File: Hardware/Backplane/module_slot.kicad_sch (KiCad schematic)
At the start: 29 parts, among them J402 10018784-10201TLF, Q401 S3134K, Q402 GSF3407, Q403 GSF3407, Q404 GSF3407, U401 NL17SZS11DFT2G-Q

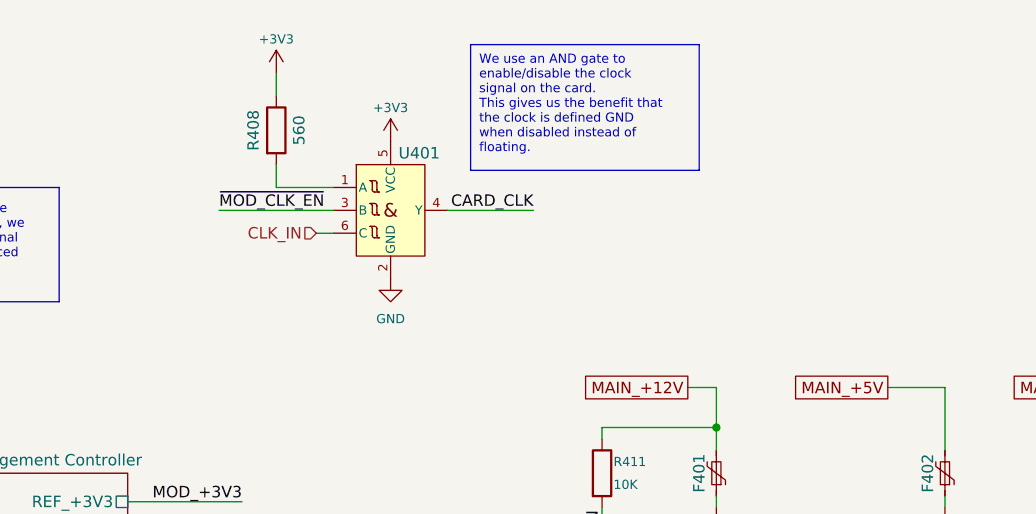
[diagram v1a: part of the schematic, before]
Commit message: Fixes several issues with the backplane schematic.
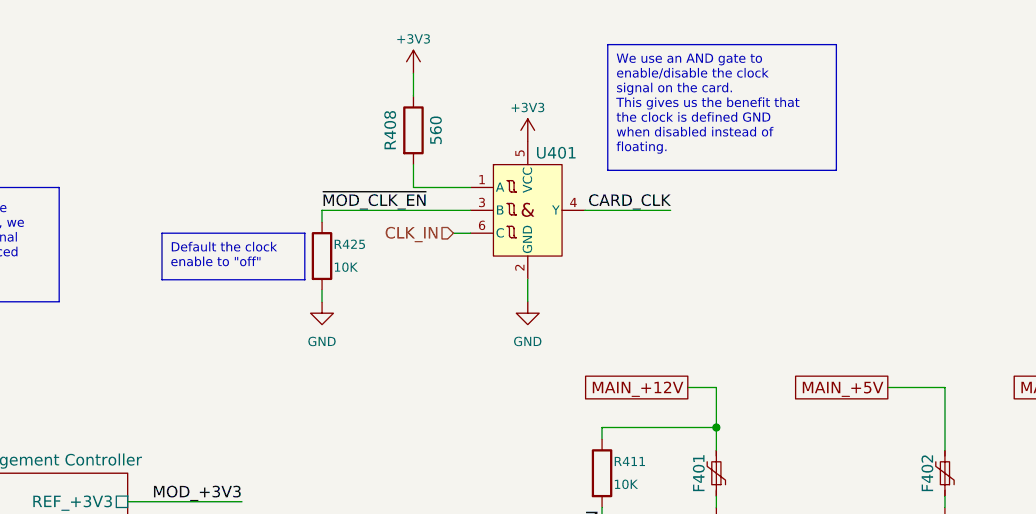
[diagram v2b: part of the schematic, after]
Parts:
- added R425: 10K, Resistor_SMD:R_0603_1608Metric, symbol Device:R
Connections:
- net GND: now also R425.2
- net ~{MOD_CLK_EN}: now also R425.1
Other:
- moved on the sheet: R408, U401

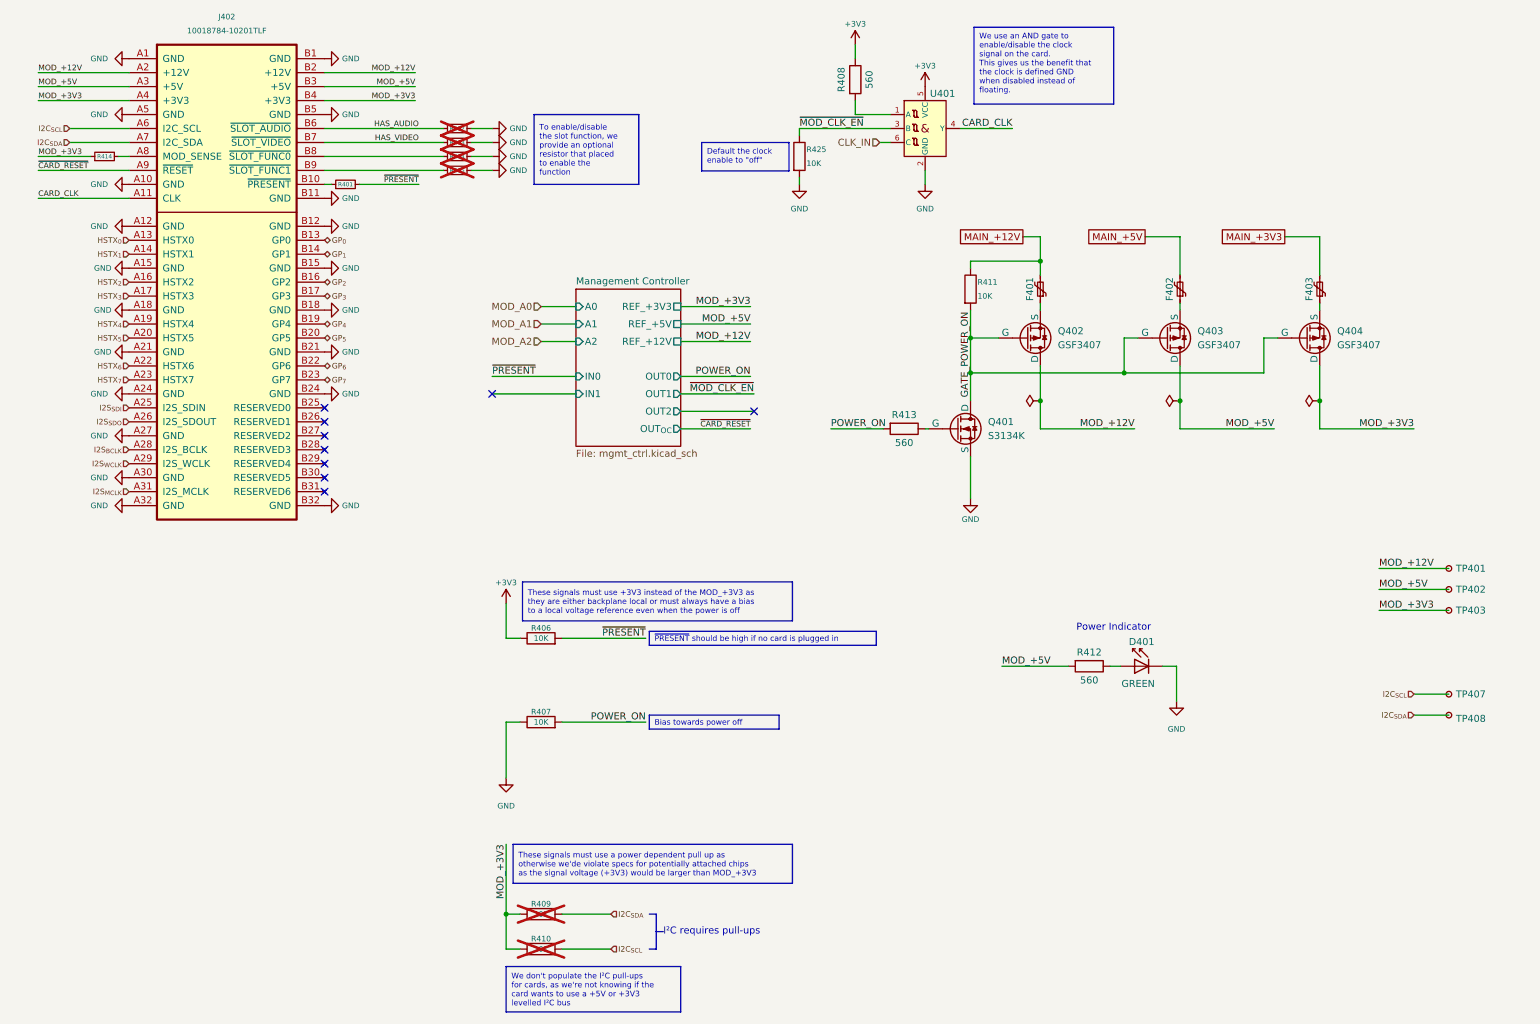
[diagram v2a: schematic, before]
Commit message: Updates the backplane to fit the new platform definition, replaces now deprecated RTC with a new one, improves power management.
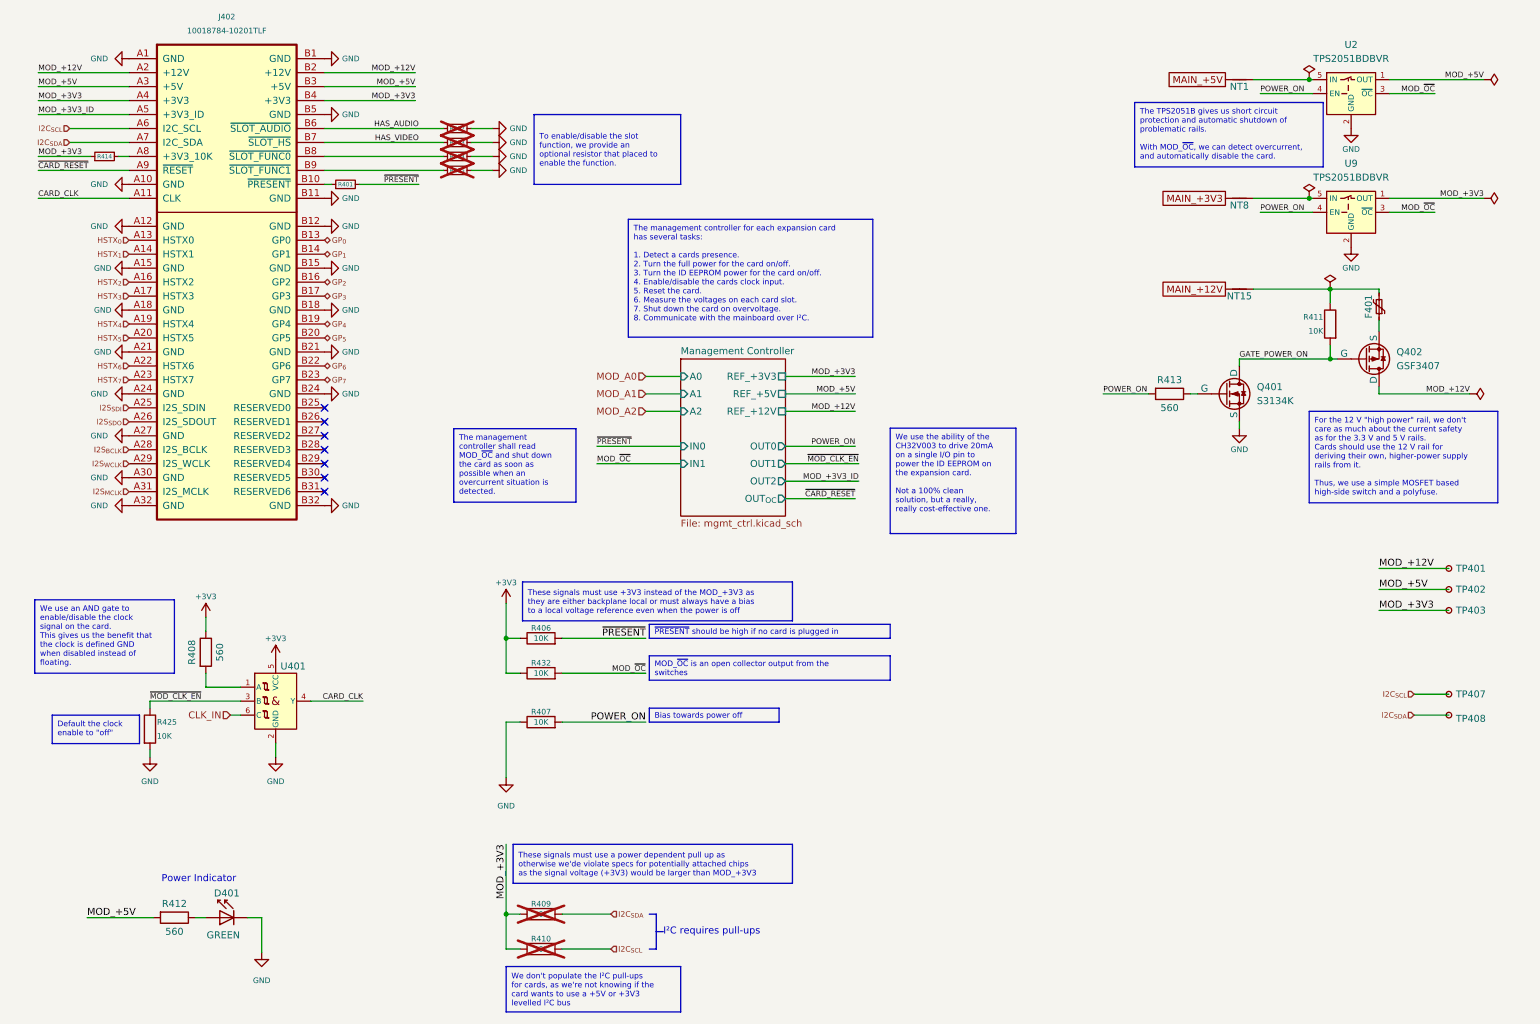
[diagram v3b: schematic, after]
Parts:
- removed F402, F403: SMD1206B050TF/15, Fuse:Fuse_1206_3216Metric, symbol Symbol Library:SMD1206B050TF/15
- removed Q403, Q404: GSF3407, Package_TO_SOT_SMD:SOT-23, symbol Home Computer:GSF3407
- added NT1, NT15, NT8: NetTie_2, NetTie:NetTie-2_SMD_Pad0.5mm, symbol Device:NetTie_2
- added R432: 10K, Resistor_SMD:R_0603_1608Metric, symbol Device:R
- added U2, U9: TPS2051BDBVR, Package_TO_SOT_SMD:SOT-23-5, symbol Home Computer:TPS2051BDBVR
- J402: symbol Home Computer:AHC-CONN-MOD -> Home Computer:AHC-CONN-EXP-HOST
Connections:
- net +3V3: now also R432.1
- net GND: now also U2.2 (GND), U9.2 (GND); no longer J402.A5 (GND)
- net MAIN_+12V: now also NT15.1; no longer F401.2, R411.1
- net MAIN_+3V3: now also NT8.1
- net MAIN_+5V: now also NT1.1
- net MOD_+3V3: now also U9.1 (OUT)
- net MOD_+5V: now also U2.1 (OUT)
- net POWER_ON: now also U2.4 (EN), U9.4 (EN)
- new net: NT1.2, U2.5 (IN)
- new net: F401.2, NT15.2, R411.1
- new net: NT8.2, U9.5 (IN)
- new net MOD_+3V3_ID: J402.A5 (+3V3_ID)
- new net MOD_~{OC}: R432.2, U2.3 (~{OC}), U9.3 (~{OC})
- no-connect marks 9 -> 7
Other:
- moved on the sheet: D401, F401, Q401, Q402, R408, R411, R412, R413, R425, U401

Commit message: Improves backplane schematic even more
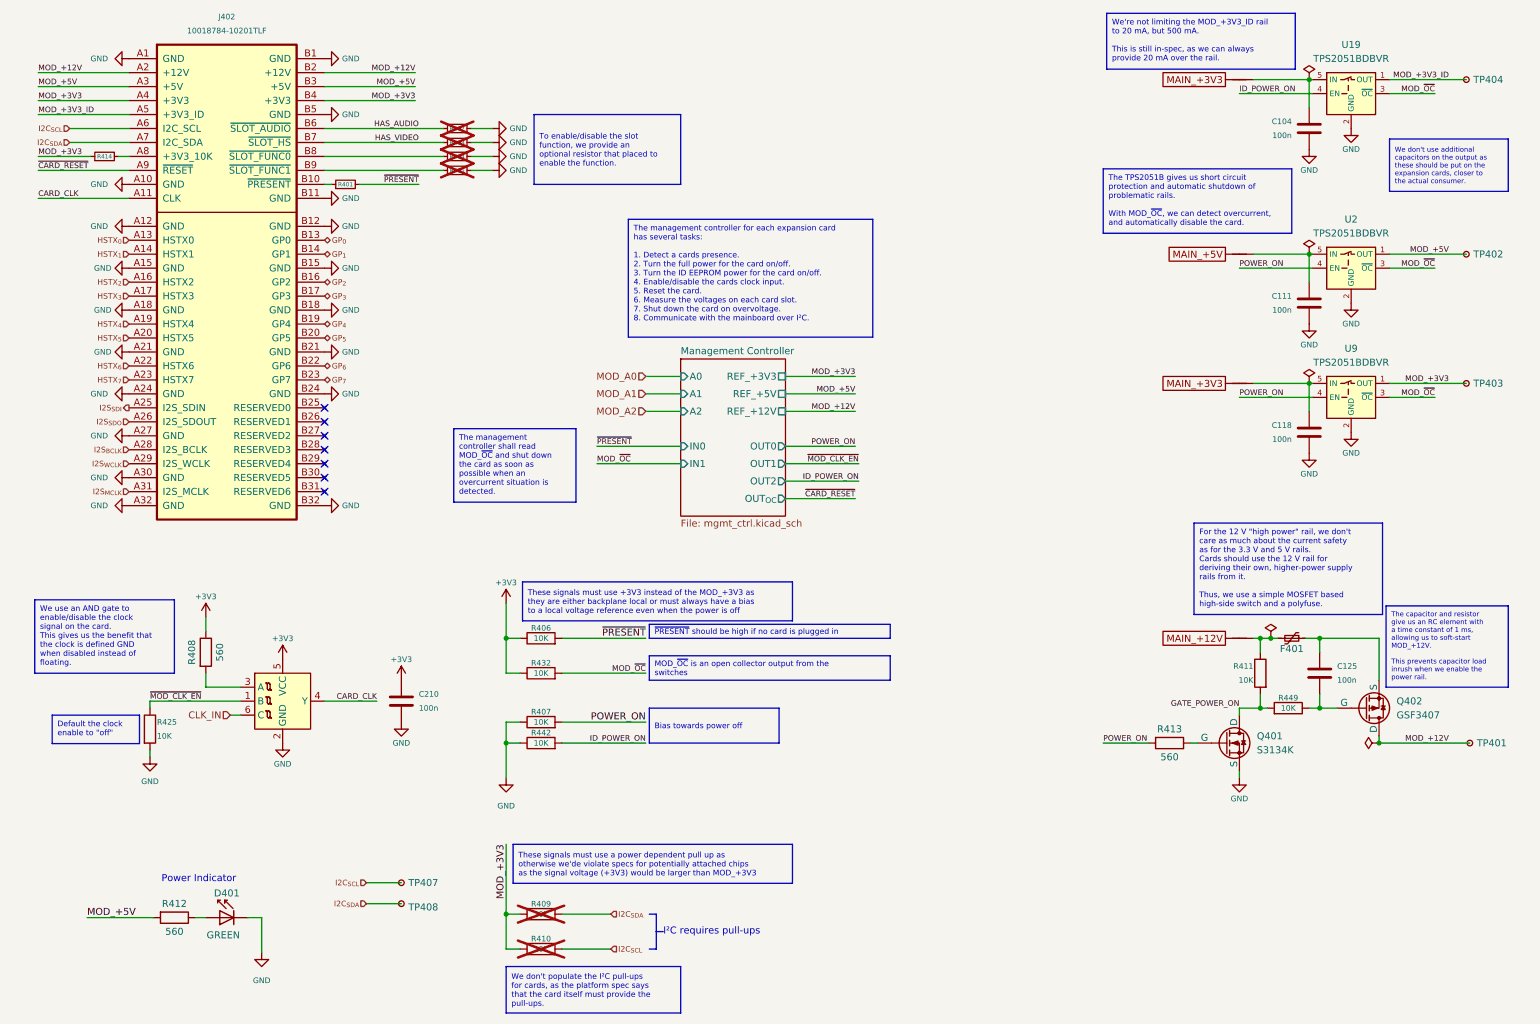
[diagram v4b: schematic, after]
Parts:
- removed U401: NL17SZS11DFT2G-Q, Package_TO_SOT_SMD:SOT-363_SC-70-6, symbol Home Computer:NL17SZS11DFT2G-Q
- added C104, C111, C118, C125, C210: 100n, Capacitor_SMD:C_0603_1608Metric, symbol Device:C
- added NT24: NetTie_2, NetTie:NetTie-2_SMD_Pad0.5mm, symbol Device:NetTie_2
- added R442, R449: 10K, Resistor_SMD:R_0603_1608Metric, symbol Device:R
- added TP404: TestPoint_Small, TestPoint:TestPoint_Pad_D1.0mm, symbol Connector:TestPoint_Small
- added U19: TPS2051BDBVR, Package_TO_SOT_SMD:SOT-23-5, symbol Home Computer:TPS2051BDBVR
- added U30: NL7SZ57DBVT1G, Package_TO_SOT_SMD:SC-74-6_1.55x2.9mm_P0.95mm, symbol Home Computer:NL7SZ57DBVT1G
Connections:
- net +3V3: now also C210.2, U30.5 (VCC)
- net CARD_CLK: now also U30.4 (Y)
- net CLK_IN: now also U30.6 (C)
- net GATE_POWER_ON: now also R449.2; no longer Q402.1 (G)
- net GND: now also C104.1, C111.1, C118.1, C210.1, R442.1, U19.2 (GND), U30.2 (GND)
- net MAIN_+3V3: now also NT24.1
- net MOD_+3V3_ID: now also TP404.1, U19.1 (OUT)
- net MOD_~{OC}: now also U19.3 (~{OC})
- net ~{MOD_CLK_EN}: now also U30.1 (B)
- net at R408.2: now also U30.3 (A)
- net at NT1.2, U2.5 (IN): now also C111.2
- net at NT8.2, U9.5 (IN): now also C118.2
- net at F401.1, Q402.2 (S): now also C125.2
- new net: C104.2, NT24.2, U19.5 (IN)
- new net: C125.1, Q402.1 (G), R449.1
- new net ID_POWER_ON: R442.2, U19.4 (EN)
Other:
- moved on the sheet: F401, Q401, Q402, R411, R413, TP401, TP402, TP403, TP407, TP408, U2, U9

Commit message: Removes useless review draft
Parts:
- renumbered C210 to C1, C104 to C2, C111 to C3, C118 to C4, C125 to C5, D401 to D1, F401 to F1, J402 to J1, NT24 to NT2, NT1 to NT3, NT8 to NT4, NT15 to NT5, Q401 to Q1, Q402 to Q2, R414 to R1, R406 to R10, R432 to R11, R407 to R12, R442 to R13, R409 to R14, R410 to R15, R413 to R16, R411 to R17, R449 to R18, R425 to R2, R412 to R3, R408 to R4, R401 to R5, R402 to R6, R403 to R7, R404 to R8, R405 to R9, TP407 to TP1, TP408 to TP2, TP404 to TP3, TP402 to TP4, TP403 to TP5, TP401 to TP6, U30 to U1, U19 to U3, U2 to U4, U9 to U5

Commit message: Starts to work on the first Backplane sub-schematic prototype
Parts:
- renumbered NT2 to NT1, NT3 to NT2, NT4 to NT3, NT5 to NT4, U3 to U2, U4 to U3, U5 to U4
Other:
- sheet Management Controller: file mgmt_ctrl.kicad_sch -> ../mgmt_ctrl.kicad_sch
